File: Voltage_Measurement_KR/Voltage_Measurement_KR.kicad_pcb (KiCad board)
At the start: 2 copper layers, 77.6 x 45 mm, 56 parts, among them IC1 MP9488GS-P, IC2 TLV1701AIDBVT, IC3 TLV1701AIDBVT, IC4 TLV1701AIDBVT, J1 Conn_01x02_Phoenix, J2 Conn_01x02_Phoenix, J3 Conn_01x03_Pin, J4 Conn_01x02_Pin, Q1 2N7000, Q2 2N7000, U1 HCPL-817-000E, U2 HCPL-817-000E, U3 HCPL-817-000E, U4 LM7805_SOT223

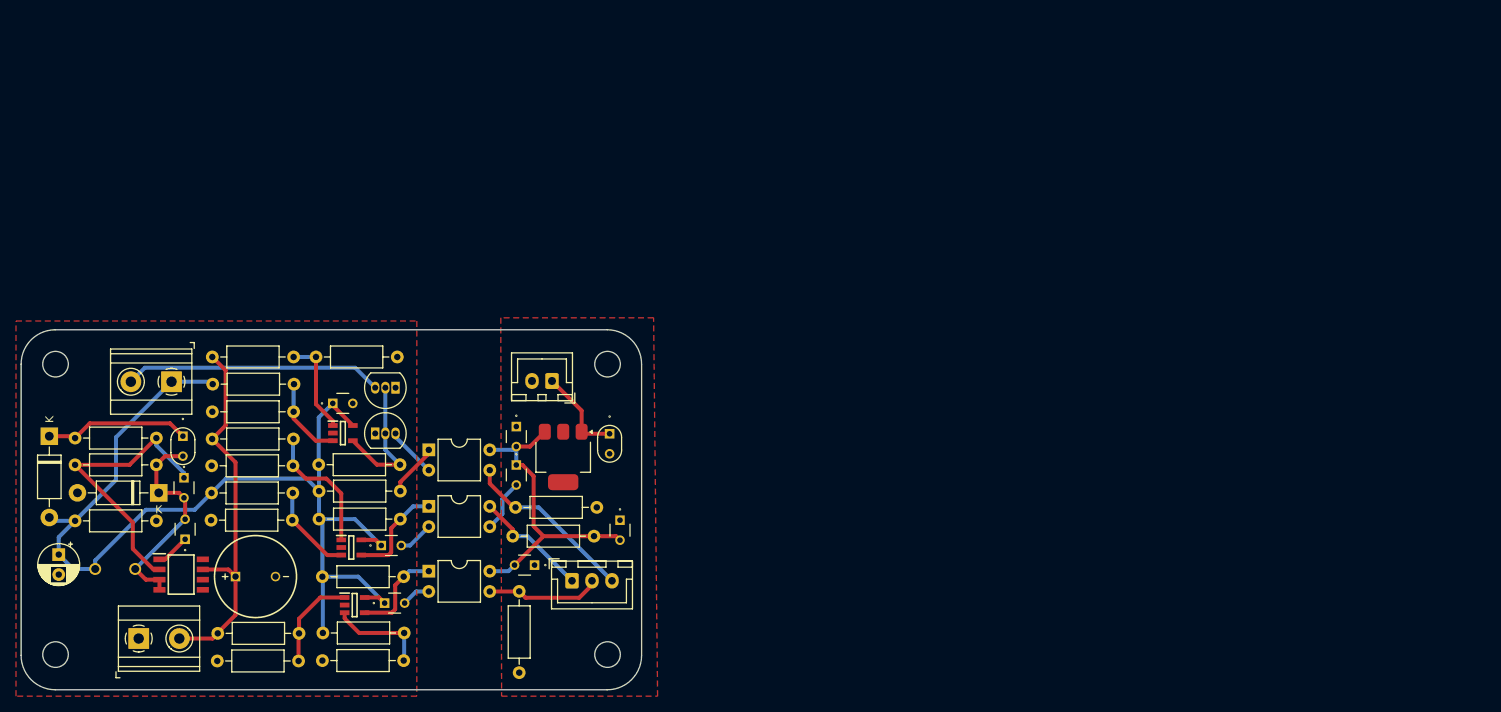
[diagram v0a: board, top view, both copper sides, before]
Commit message: Voltage measurement completed
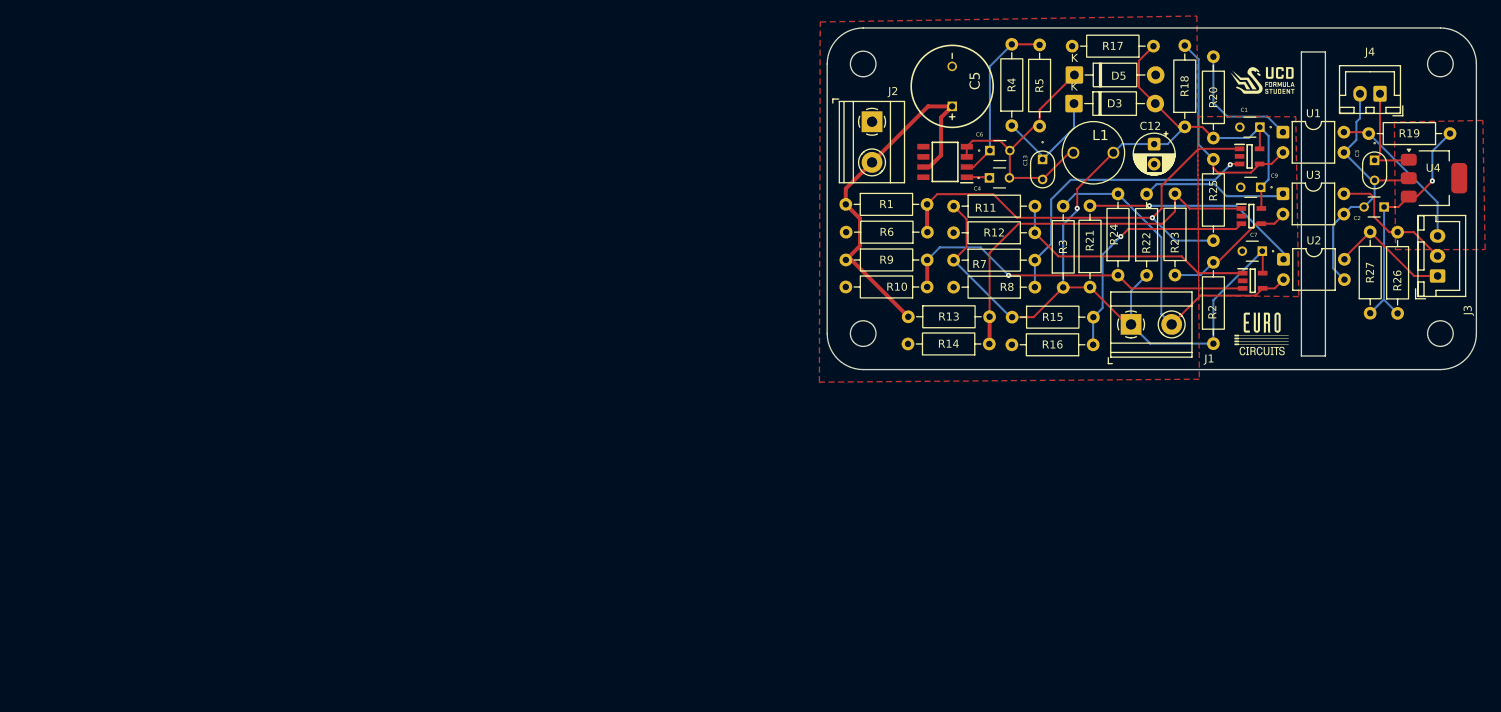
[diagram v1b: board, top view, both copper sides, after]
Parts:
- removed C10, C11, C14: 0.1uF, FA14_Capacitor:FA18X7R1H104KNU00
- removed Q1, Q2: 2N7000, Package_TO_SOT_THT:TO-92_Inline
- removed the REF** at (141.4, 121.6)
- removed the REF** at (72.4, 121.6)
- removed the REF** at (141.4, 85.3)
- removed the REF** at (72.4, 85.3)
- added R21: 2.2K, Resistor_THT:R_Axial_DIN0207_L6.3mm_D2.5mm_P10.16mm_Horizontal, F.Cu at (201.8, 75.7)
- added R22: 2.2K, Resistor_THT:R_Axial_DIN0207_L6.3mm_D2.5mm_P10.16mm_Horizontal, F.Cu at (208.8, 74.2)
- added R23: 1.5M, Resistor_THT:R_Axial_DIN0207_L6.3mm_D2.5mm_P10.16mm_Horizontal, F.Cu at (212.4, 64.0)
- added R24: 1.5M, Resistor_THT:R_Axial_DIN0207_L6.3mm_D2.5mm_P10.16mm_Horizontal, F.Cu at (205.2, 74.2)
- added R25: 1.5M, Resistor_THT:R_Axial_DIN0207_L6.3mm_D2.5mm_P10.16mm_Horizontal, F.Cu at (217.2, 69.9)
- added REF**: MountingHole_3.2mm_M3, MountingHole:MountingHole_3.2mm_M3, F.Cu at (173.4, 81.5)
- added REF**: MountingHole_3.2mm_M3, MountingHole:MountingHole_3.2mm_M3, F.Cu at (245.6, 81.5)
- added REF**: MountingHole_3.2mm_M3, MountingHole:MountingHole_3.2mm_M3, F.Cu at (245.6, 47.8)
- added REF**: MountingHole_3.2mm_M3, MountingHole:MountingHole_3.2mm_M3, F.Cu at (173.4, 47.8)
- R18, R2, R3: value 1K -> 100K
- R19, R26, R27: value 1K -> 10K
- R20: value 1K -> 2.2K
- moved R17 147.3 mm to (209.7, 45.5), turned to 180 degrees
- moved C12 146.2 mm to (209.8, 57.8)
- moved D3 134.7 mm to (199.8, 52.7), turned to 0 degrees
- moved L1 132.9 mm to (202.2, 58.9), turned to 180 degrees
- moved R5 131.5 mm to (195.4, 45.4), turned to -90 degrees
- moved R19 125.8 mm to (246.8, 56.5), turned to 180 degrees
- moved D5 125.8 mm to (199.8, 49.1), turned to 0 degrees
- moved R4 123.4 mm to (192.0, 55.5), turned to 90 degrees
- moved IC4 122.2 mm to (221.9, 66.8)
- moved C9 121.2 mm to (223.1, 63.2), turned to 180 degrees
- moved C1 120.9 mm to (223.0, 55.7), turned to 180 degrees
- moved J1 120.2 mm to (206.9, 80.3), turned to 0 degrees
- moved IC2 118.5 mm to (221.7, 59.3)
- moved IC3 117.5 mm to (222.1, 74.9)
- moved U3 116.7 mm to (225.9, 64.0)
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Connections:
- IC3 pad 1: 300V_REF_2 -> 60V_REF_2
- IC3 pad 3: 60V_REF_2 -> 300V_REF_2
- IC3 pad 4: Net-(IC3-OUT) -> LED-
- R19 pad 1: TS>60V (1) -> 5V
- R19 pad 2: GLV- -> TS>60V (1)
- R26 pad 1: TS>60V (2) -> 5V
- R26 pad 2: GLV- -> TS>60V (2)
- R3 pad 2: Net-(IC3-OUT) -> LED-
- U1 pad 2: Net-(Q2-D) -> Net-(IC2-OUT)
- U1 pad 3: TS>60V (1) -> GLV-
- U1 pad 4: 5V -> TS>60V (1)
- U2 pad 1: Net-(IC3-OUT) -> Net-(R21-Pad2)
- U2 pad 2: TS- -> LED-
- U3 pad 1: Net-(IC4-OUT) -> Net-(R22-Pad2)
- U3 pad 2: TS- -> Net-(IC4-OUT)
- U3 pad 3: TS>60V (2) -> GLV-
- U3 pad 4: 5V -> TS>60V (2)
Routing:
- net 300V_REF_1: track 12.2 -> 58.4 mm, vias 0 -> 1
- net 300V_REF_3: track 12.1 -> 48.0 mm
- net 300V_REF_2: track 16.7 -> 45.6 mm, vias 0 -> 1
- net Net-(R21-Pad2): track 0.00 -> 27.4 mm, vias 0 -> 1
- net GLV-: track 6.59 -> 33.9 mm
- net 60V_REF_1: track 10.4 -> 37.2 mm, vias 0 -> 1
- net 60V_REF_2: track 11.4 -> 31.4 mm
- net 60V_REF_3: track 12.4 -> 30.7 mm, vias 0 -> 1
- net Net-(R22-Pad2): track 0.00 -> 18.3 mm
- net Net-(IC1-FB): track 35.8 -> 21.7 mm
- net Net-(IC3-OUT): track 12.7 -> 0.00 mm
- net LED-: track 32.3 -> 42.9 mm
- net Net-(R20-Pad1): track 6.63 -> 16.0 mm
- net Net-(IC2-OUT): track 17.5 -> 26.8 mm
- net 5V: track 39.2 -> 30.7 mm, vias 0 -> 1
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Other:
- board size 77.6 x 45 mm -> 81.2 x 42.7 mm

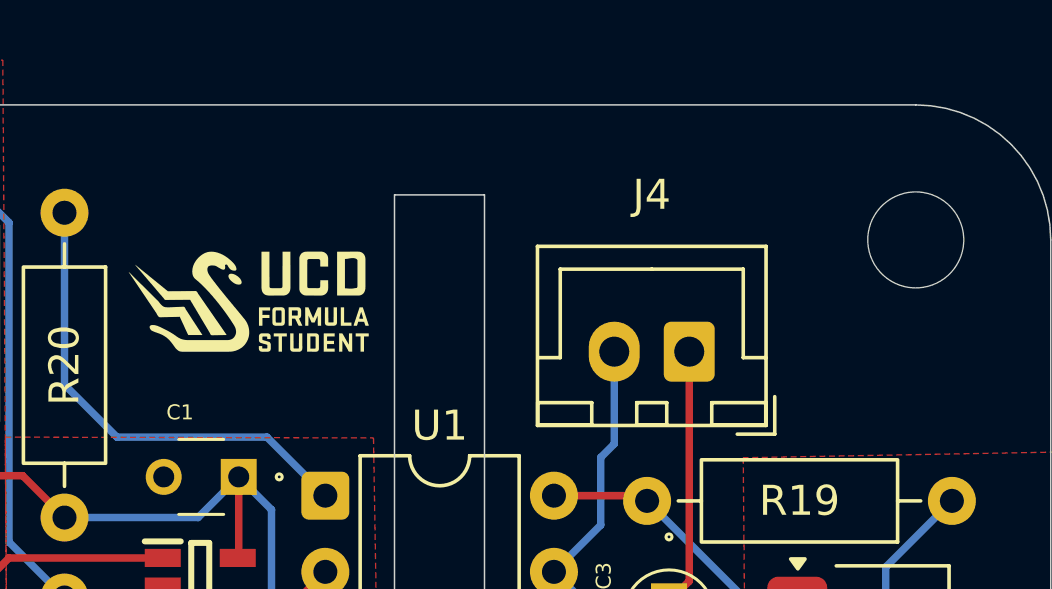
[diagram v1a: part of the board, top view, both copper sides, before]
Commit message: added HVLV labels
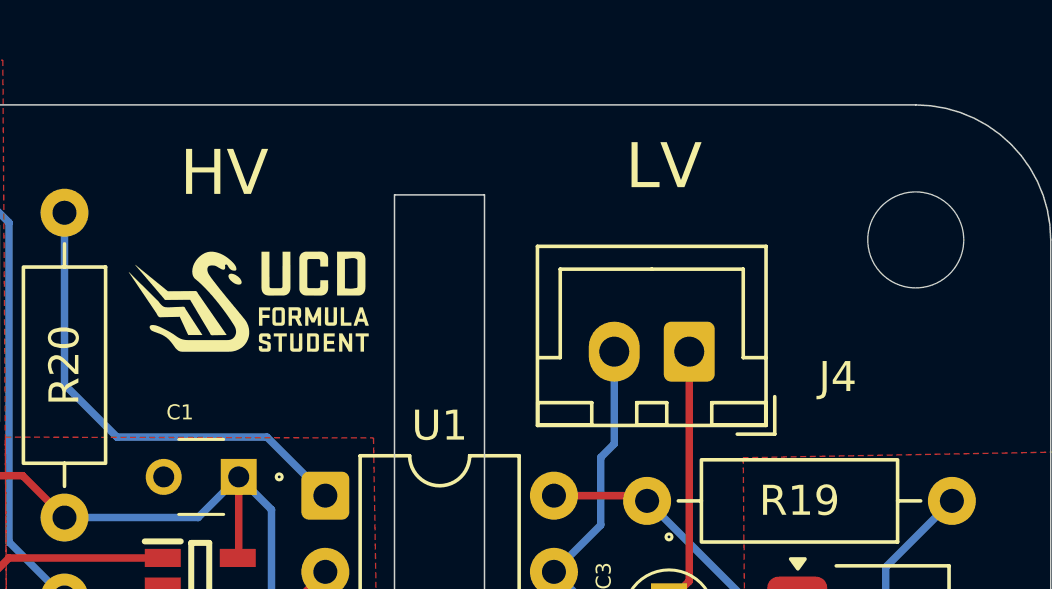
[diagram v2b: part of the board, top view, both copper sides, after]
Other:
- board text added: "HV"
- board text added: "LV"
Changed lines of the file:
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@@
 		(tags "connector JST XH vertical")
 		(property "Reference" "J4"
-			(at 1.25 5.225 0)
+			(at -4.95 -0.85 0)
 			(layer "F.SilkS")
 			(effects
@@
 		(layer "Edge.Cuts")
 	)
+	(gr_text "HV"
+		(at 221.025 46.425 0)
+		(layer "F.SilkS")
+		(effects
+			(font
+				(size 1.5 1.5)
+				(thickness 0.15)
+			)
+			(justify left bottom)
+		)
+	)
+	(gr_text "LV"
+		(at 235.875 46.2 0)
+		(layer "F.SilkS")
+		(effects
+			(font
+				(size 1.5 1.5)
+				(thickness 0.15)
+			)
+			(justify left bottom)
+		)
+	)
 	(segment
